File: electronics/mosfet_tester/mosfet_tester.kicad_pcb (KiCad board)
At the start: 2 copper layers, 77 parts, among them J102 CONN_01X06, J103 Screw_Terminal_1x01, J104 Screw_Terminal_1x01, J201 TEST_1P, J202 TEST_1P, J203 TEST_1P, J204 TEST_1P, J205 TEST_1P, J206 TEST_1P, J207 TEST_1P, J301 TEST_1P, J302 TEST_1P, J303 TEST_1P, J304 TEST_1P, J305 TEST_1P, J306 TEST_1P, J307 TEST_1P, J401 TEST_1P, J402 TEST_1P, J403 TEST_1P, J404 TEST_1P, J405 TEST_1P, J406 TEST_1P, J407 TEST_1P, J501 TEST_1P, J502 TEST_1P, J503 TEST_1P, J504 TEST_1P, J505 TEST_1P, J506 TEST_1P, J507 TEST_1P, Q201 Q_NMOS_GSD, Q301 Q_NMOS_GSD, Q401 Q_NMOS_GSD, Q501 Q_NMOS_GSD, U201 LM358, U301 LM358, U401 LM358, U501 LM358

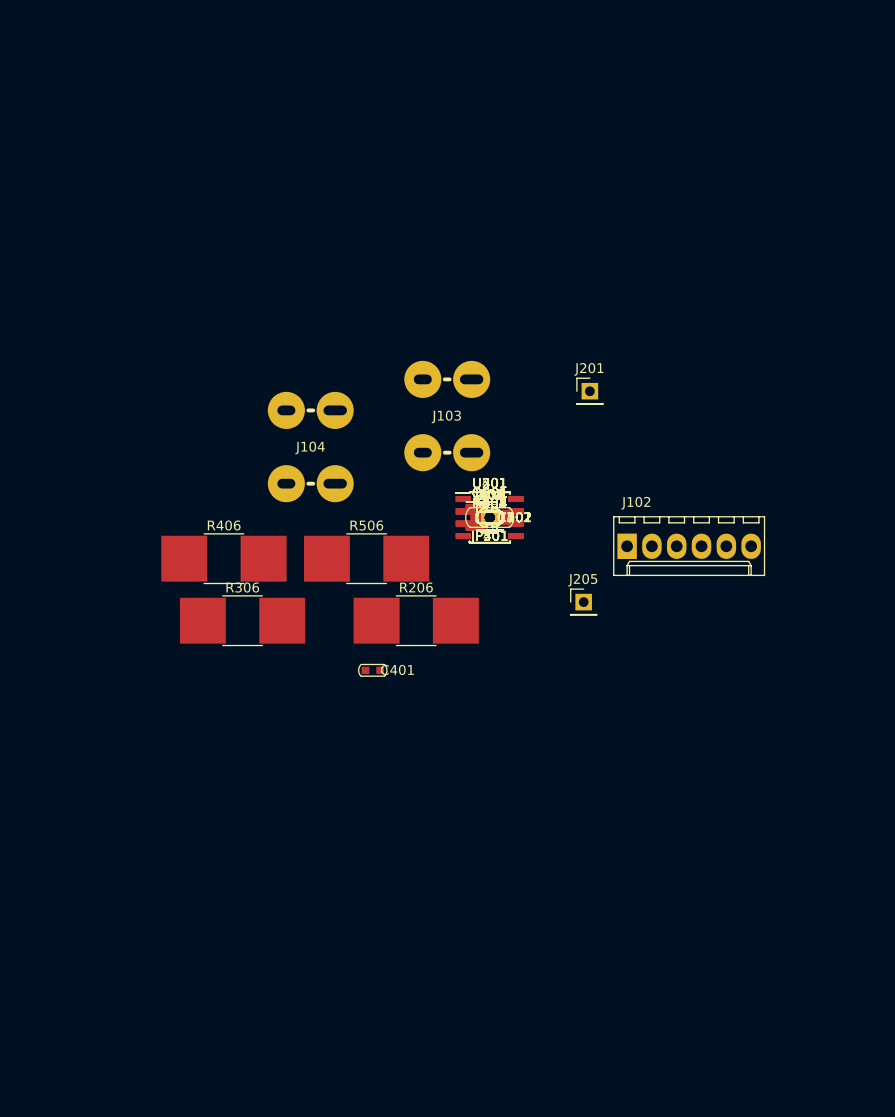
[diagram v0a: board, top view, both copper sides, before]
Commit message: mosfet tester progress
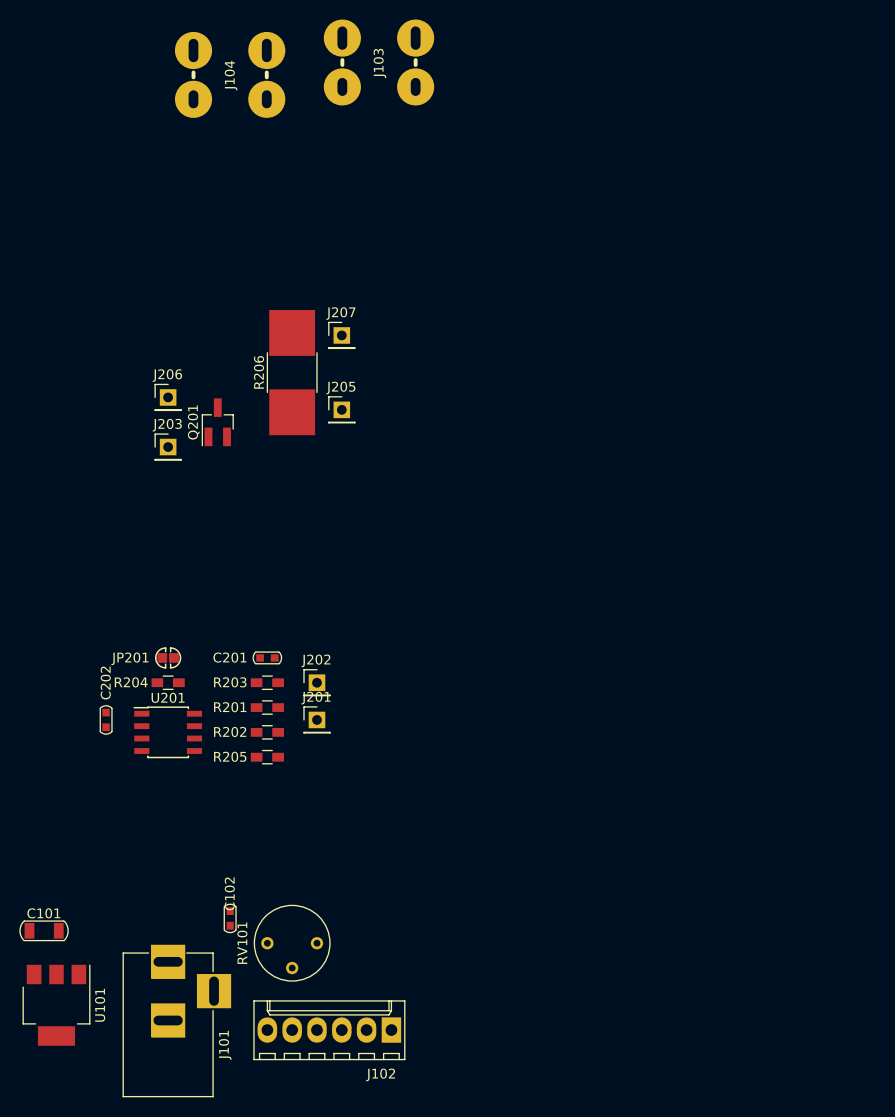
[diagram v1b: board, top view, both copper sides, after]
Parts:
- removed C301, C401, C501: 0.1, Capacitors_SMD_Round:C_0603
- removed C302, C402, C502: C, Capacitors_SMD_Round:C_0603
- removed J204, J301, J302, J303, J304, J305, J306, J307, J401, J402, J403, J404, J405, J406, J407, J501, J502, J503, J504, J505, J506, J507: TEST_1P, Pin_Headers:Pin_Header_Straight_1x01_Pitch2.54mm
- removed JP301, JP401, JP501: Jumper_NC_Small, SolderJumpers:SJ_1_NO
- removed Q301, Q401, Q501: Q_NMOS_GSD, TO_SOT_Packages_SMD:SOT-23_Handsoldering
- removed R301, R401, R501: 100R, Resistors_SMD:R_0603_HandSoldering
- removed R302, R303, R304, R305, R402, R403, R404, R405, R502, R503, R504, R505: R, Resistors_SMD:R_0603_HandSoldering
- removed R306, R406, R506: R, Resistors_SMD:R_2816_HandSoldering
- removed U301, U401, U501: LM358, Housings_SOIC:SOIC-8_3.9x4.9mm_Pitch1.27mm
- added J101: BARREL_JACK, Connectors:BARREL_JACK, F.Cu at (115.6, 150.5)
- added RV101: 10K, Potentiometers:Potentiometer_Trimmer_Bourns_3339P_Horizontal, F.Cu at (130.8, 148.6)
- added U101: LM7805CT, TO_SOT_Packages_SMD:SOT-223-3Lead_TabPin2, F.Cu at (104.1, 154.9)
- C102: value C -> 0.1
- moved C101 62.2 mm to (102.9, 147.3)
- moved J102 55.1 mm to (138.4, 157.5), turned to 180 degrees
- moved C102 48.9 mm to (121.9, 146.1), turned to 90 degrees
- moved C202 44.4 mm to (109.2, 125.7), turned to 270 degrees
- moved J201 43.7 mm to (130.8, 125.7)
- moved U201 39.6 mm to (115.6, 127.0)
- moved J104 39.0 mm to (121.9, 59.7), turned to 90 degrees
- moved R204 37.0 mm to (115.6, 121.9), turned to 180 degrees
- moved J103 36.9 mm to (137.2, 58.4), turned to 90 degrees
- moved JP201 35.9 mm to (115.6, 119.4), turned to 180 degrees
- moved J206 35.2 mm to (115.6, 92.7)
- moved J203 33.7 mm to (115.6, 97.8)
- moved R205 33.5 mm to (125.7, 129.5), turned to 180 degrees
- moved R202 31.7 mm to (125.7, 127.0), turned to 180 degrees
- moved J205 31.6 mm to (133.3, 94.0)
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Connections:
- net /sheet59556740/5V_REF renamed /slice/5V_REF
- C101 pad 1: (no net) -> +5V
- J102 pad 2: /sheet59556740/Vgs -> (no net)
- J102 pad 3: /sheet59556CDB/Vgs -> (no net)
- J102 pad 4: /sheet5955708A/Vgs -> (no net)
- J103 pad 1: /sheet59556740/VIN- -> GND
- J104 pad 1: /sheet59556740/VIN+ -> /slice/VIN+
- J205 pad 1: (no net) -> Net-(J205-Pad1)
- J206 pad 1: (no net) -> /slice/VIN+
- J207 pad 1: (no net) -> GND
- JP201 pad 2: /sheet59556740/VIN- -> GND
- Q201 pad 2: Net-(Q201-Pad2) -> Net-(J205-Pad1)
- Q201 pad 3: /sheet59556740/VIN+ -> /slice/VIN+
- R205 pad 1: Net-(Q201-Pad2) -> Net-(J205-Pad1)
- R206 pad 1: Net-(Q201-Pad2) -> Net-(J205-Pad1)
- R206 pad 2: /sheet59556740/VIN- -> GND

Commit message: Rework entire board, still in progress
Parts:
- removed J206, J207: TEST_1P, Pin_Headers:Pin_Header_Straight_1x01_Pitch2.54mm
- removed JP201: Jumper_NC_Small, SolderJumpers:SJ_1_NO
- added C102: 0.1u, Capacitors_SMD_Round:C_0603, F.Cu at (135.3, 123.2)
- added C301: 0.1, Capacitors_SMD_Round:C_0603, F.Cu at (141.6, 108.0)
- added C302: C, Capacitors_SMD_Round:C_0603, F.Cu at (137.8, 100.3)
- added C401: 0.1, Capacitors_SMD_Round:C_0603, F.Cu at (157.5, 108.0)
- added C402: C, Capacitors_SMD_Round:C_0603, F.Cu at (153.7, 100.3)
- added C501: 0.1, Capacitors_SMD_Round:C_0603, F.Cu at (174.0, 108.0)
- added C502: C, Capacitors_SMD_Round:C_0603, F.Cu at (170.2, 100.3)
- added J301: TEST_1P, Pin_Headers:Pin_Header_Straight_1x01_Pitch2.54mm, F.Cu at (142.2, 113.0)
- added J302: TEST_1P, Pin_Headers:Pin_Header_Straight_1x01_Pitch2.54mm, F.Cu at (147.3, 113.0)
- added J303: TEST_1P, Pin_Headers:Pin_Header_Straight_1x01_Pitch2.54mm, F.Cu at (142.2, 118.7)
- added J304: TEST_1P, Pin_Headers:Pin_Header_Straight_1x01_Pitch2.54mm, F.Cu at (147.3, 118.7)
- added J401: TEST_1P, Pin_Headers:Pin_Header_Straight_1x01_Pitch2.54mm, F.Cu at (158.1, 113.0)
- added J402: TEST_1P, Pin_Headers:Pin_Header_Straight_1x01_Pitch2.54mm, F.Cu at (163.2, 113.0)
- added J403: TEST_1P, Pin_Headers:Pin_Header_Straight_1x01_Pitch2.54mm, F.Cu at (158.1, 118.7)
- added J404: TEST_1P, Pin_Headers:Pin_Header_Straight_1x01_Pitch2.54mm, F.Cu at (163.2, 118.7)
- added J501: TEST_1P, Pin_Headers:Pin_Header_Straight_1x01_Pitch2.54mm, F.Cu at (174.6, 113.0)
- added J502: TEST_1P, Pin_Headers:Pin_Header_Straight_1x01_Pitch2.54mm, F.Cu at (179.7, 113.0)
- added J503: TEST_1P, Pin_Headers:Pin_Header_Straight_1x01_Pitch2.54mm, F.Cu at (174.6, 118.7)
- added J504: TEST_1P, Pin_Headers:Pin_Header_Straight_1x01_Pitch2.54mm, F.Cu at (179.7, 118.7)
- added P101: OSHW, Symbols:OSHW-Logo_7.5x8mm_SilkScreen, F.Cu at (137.2, 93.3)
- added Q301: Q_NMOS_GSD, TO_Combo_Packages:TO_220_247, F.Cu at (141.6, 79.4)
- added Q401: Q_NMOS_GSD, TO_Combo_Packages:TO_220_247, B.Cu at (157.5, 79.4)
- added Q501: Q_NMOS_GSD, TO_Combo_Packages:TO_220_247, F.Cu at (174.0, 79.4)
- added R101: 0R, Resistors_SMD:R_0805_HandSoldering, F.Cu at (186.1, 97.8)
- added R301: 100R, Resistors_SMD:R_0603_HandSoldering, F.Cu at (148.0, 101.6)
- added R302: R, Resistors_SMD:R_0603_HandSoldering, F.Cu at (148.0, 103.5)
- added R303: R, Resistors_SMD:R_0603_HandSoldering, F.Cu at (148.0, 105.4)
- added R304: R, Resistors_THT:R_Axial_DIN0207_L6.3mm_D2.5mm_P10.16mm_Horizontal, F.Cu at (144.8, 89.5)
- added R305: R, Resistors_THT:R_Axial_DIN0207_L6.3mm_D2.5mm_P10.16mm_Horizontal, F.Cu at (148.0, 89.5)
- added R306: R, Resistors_SMD:R_2816_HandSoldering, F.Cu at (146.1, 85.7)
- added R401: 100R, Resistors_SMD:R_0603_HandSoldering, F.Cu at (163.8, 101.6)
- added R402: R, Resistors_SMD:R_0603_HandSoldering, F.Cu at (163.8, 103.5)
- added R403: R, Resistors_SMD:R_0603_HandSoldering, F.Cu at (163.8, 105.4)
- added R404: R, Resistors_THT:R_Axial_DIN0207_L6.3mm_D2.5mm_P10.16mm_Horizontal, F.Cu at (160.7, 89.5)
- added R405: R, Resistors_THT:R_Axial_DIN0207_L6.3mm_D2.5mm_P10.16mm_Horizontal, F.Cu at (163.8, 89.5)
- added R406: R, Resistors_SMD:R_2816_HandSoldering, F.Cu at (161.9, 85.7)
- added R501: 100R, Resistors_SMD:R_0603_HandSoldering, F.Cu at (181.0, 101.6)
- added R502: R, Resistors_SMD:R_0603_HandSoldering, F.Cu at (181.0, 103.5)
- added R503: R, Resistors_SMD:R_0603_HandSoldering, F.Cu at (181.0, 105.4)
- added R504: R, Resistors_THT:R_Axial_DIN0207_L6.3mm_D2.5mm_P10.16mm_Horizontal, F.Cu at (177.2, 89.5)
- added R505: R, Resistors_THT:R_Axial_DIN0207_L6.3mm_D2.5mm_P10.16mm_Horizontal, F.Cu at (180.3, 89.5)
- added R506: R, Resistors_SMD:R_2816_HandSoldering, F.Cu at (178.4, 85.7)
- added U301: LM358, Housings_SOIC:SOIC-8_3.9x4.9mm_Pitch1.27mm, F.Cu at (141.6, 104.1)
- added U401: LM358, Housings_SOIC:SOIC-8_3.9x4.9mm_Pitch1.27mm, F.Cu at (157.5, 104.1)
- added U501: LM358, Housings_SOIC:SOIC-8_3.9x4.9mm_Pitch1.27mm, F.Cu at (174.0, 104.1)
- C101: value C -> 22u
- J102: value CONN_01X06 -> CONN_01X03; footprint Connectors_Molex:Molex_KK-6410-06_06x2.54mm_Straight -> Connectors_Molex:Molex_KK-6410-03_03x2.54mm_Straight
- J103, J104: footprint Screw_Connectors:4_Pin_Screw_Connector -> Screw_Connectors:2_Pin_Quick_Fit
- Q201: footprint TO_SOT_Packages_SMD:SOT-23_Handsoldering -> TO_Combo_Packages:TO_220_247; moved to B.Cu
- R204, R205: footprint Resistors_SMD:R_0603_HandSoldering -> Resistors_THT:R_Axial_DIN0207_L6.3mm_D2.5mm_P10.16mm_Horizontal
- RV101: footprint Potentiometers:Potentiometer_Trimmer_Bourns_3339P_Horizontal -> Potentiometers:Potentiometer_Alps_RK163_Double_Vertical
- U101: value LM7805CT -> MCP1703A-3302/MB; footprint TO_SOT_Packages_SMD:SOT-223-3Lead_TabPin2 -> TO_SOT_Packages_SMD:SOT89-3_Housing
- moved J102 43.5 mm to (120.0, 118.1), turned to 90 degrees
- moved U101 40.6 mm to (135.3, 128.9), turned to 180 degrees
- moved R205 40.5 mm to (132.1, 89.5), turned to 270 degrees
- moved C101 39.3 mm to (135.3, 125.1), turned to 180 degrees
- moved J104 36.2 mm to (122.6, 95.9), turned to 0 degrees
- moved R204 35.0 mm to (128.9, 89.5), turned to 270 degrees
- moved J103 33.9 mm to (120.0, 87.6), turned to 270 degrees
- moved C202 28.4 mm to (121.9, 100.3), turned to 180 degrees
- moved C103 25.5 mm to (142.9, 131.4)
- moved U201 25.0 mm to (125.7, 104.1)
- moved J204 24.8 mm to (131.4, 118.7)
- moved J101 24.7 mm to (126.4, 128.3), turned to 0 degrees
- moved R202 24.3 mm to (132.1, 103.5)
- moved R201 23.7 mm to (132.1, 101.6)
- moved J203 23.6 mm to (126.4, 118.7)
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- renumbered C102 to C103, J205 to J204
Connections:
- C103 pad 1: /slice/5V_REF -> /slice1/5V_REF
- C202 pad 1: Net-(C202-Pad1) -> /slice1/Vgs
- J102 pad 1: /slice/Vgs -> +12V
- J102 pad 2: (no net) -> /slice1/5V_REF
- J102 pad 3: (no net) -> GND
- J103 pad 1: GND -> /slice1/VIN+
- J104 pad 1: /slice/VIN+ -> /slice1/VIN-
- J203 pad 1: /slice/Vgs -> /slice1/Vgs
- J204 pad 1: Net-(J205-Pad1) -> Net-(J204-Pad1)
- Q201 pad 1: /slice/Vgs -> Net-(Q201-Pad1)
- Q201 pad 2: Net-(J205-Pad1) -> Net-(Q201-Pad2)
- Q201 pad 3: /slice/VIN+ -> /slice1/VIN+
- R203 pad 1: Net-(JP201-Pad1) -> /slice1/VIN-
- R204 pad 1: /slice/Vgs -> Net-(Q201-Pad2)
- R204 pad 2: Net-(C202-Pad1) -> Net-(J204-Pad1)
- R205 pad 1: Net-(J205-Pad1) -> Net-(Q201-Pad1)
- R205 pad 2: Net-(R205-Pad2) -> /slice1/Vgs
- R206 pad 1: Net-(J205-Pad1) -> Net-(Q201-Pad2)
- R206 pad 2: GND -> /slice1/VIN-
- RV101 pad 2: /slice/5V_REF -> /slice1/5V_REF
- U101 pad 1: +12V -> GND
- U101 pad 2: GND -> +12V
- U201 pad 1: Net-(C202-Pad1) -> /slice1/Vgs
- U201 pad 3: /slice/5V_REF -> /slice1/5V_REF
- U201 pad 5: Net-(R205-Pad2) -> Net-(J204-Pad1)
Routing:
- net +12V: track 0.00 -> 111.5 mm, vias 0 -> 4
- net /slice1/5V_REF: track 0.00 -> 106.8 mm, vias 0 -> 2
- net /slice1/VIN+: track 0.00 -> 96.7 mm
- net GND: track 0.00 -> 69.2 mm
- net /slice1/VIN-: track 0.00 -> 34.1 mm
- net /slice1/Vgs: track 0.00 -> 30.0 mm, vias 0 -> 1
- net /slice2/Vgs: track 0.00 -> 29.5 mm, vias 0 -> 1
- net /slice3/Vgs: track 0.00 -> 29.5 mm, vias 0 -> 1
- net /slice4/Vgs: track 0.00 -> 29.5 mm, vias 0 -> 1
- net Net-(C502-Pad2): track 0.00 -> 23.0 mm, vias 0 -> 1
- net Net-(J404-Pad1): track 0.00 -> 22.9 mm, vias 0 -> 1
- net Net-(J204-Pad1): track 0.00 -> 22.9 mm, vias 0 -> 1
- net Net-(C202-Pad2): track 0.00 -> 22.6 mm, vias 0 -> 1
- net Net-(C402-Pad2): track 0.00 -> 22.3 mm, vias 0 -> 1
- net Net-(C302-Pad2): track 0.00 -> 22.3 mm, vias 0 -> 1
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- added copper zone on B.Cu, net /slice1/VIN+
- added copper zone on F.Cu, net /slice1/VIN-
- added copper zone on F.Cu, net GND
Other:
- board outline added: 71.8 x 60.3 mm

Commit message: Checkpoint mosfet tester
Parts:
- removed J102: CONN_01X03, Connectors_Molex:Molex_KK-6410-03_03x2.54mm_Straight
- removed U101: MCP1703A-3302/MB, TO_SOT_Packages_SMD:SOT89-3_Housing
- added J1: CONN_01X03, Connectors_Molex:Molex_KK-6410-03_03x2.54mm_Straight, F.Cu at (120.0, 116.2)
- added M1: BuckModule, Buck_Modules:Buck_Module_7805_Replacement_Universal, F.Cu at (167.0, 123.2)
- moved C101 34.7 mm to (168.9, 116.8)
- moved P101 31.1 mm to (136.5, 124.5)
- moved C102 19.3 mm to (153.7, 117.5)
- moved C103 19.2 mm to (153.7, 115.6), turned to 0 degrees
- moved RV101 5.71 mm to (148.0, 127.6)
- moved J101 4.45 mm to (126.4, 123.8)
- moved J203 1.91 mm to (126.4, 116.8)
- moved J204 1.91 mm to (131.4, 116.8)
- moved J303 1.91 mm to (142.2, 116.8)
- moved J304 1.91 mm to (147.3, 116.8)
- moved J403 1.91 mm to (158.1, 116.8)
- moved J404 1.91 mm to (163.2, 116.8)
- moved J503 1.91 mm to (174.6, 116.8)
- moved J504 1.91 mm to (179.7, 116.8)
- moved J201 1.27 mm to (126.4, 111.8)
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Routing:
- net GND: track 69.2 -> 13.1 mm
- net +12V: track 111.5 -> 143.4 mm
- net /slice1/5V_REF: track 106.8 -> 90.8 mm, vias 2 -> 3
- net +5V: track 18.2 -> 33.0 mm, vias 0 -> 1
- net /slice1/VIN+: track 96.7 -> 103.6 mm
- net Net-(J504-Pad1): track 21.6 -> 19.7 mm
- net Net-(J404-Pad1): track 22.9 -> 21.0 mm
- net Net-(J304-Pad1): track 22.0 -> 20.1 mm
- net Net-(J204-Pad1): track 22.9 -> 21.0 mm
- net /slice4/Vgs: track 29.5 -> 27.6 mm
- net /slice3/Vgs: track 29.5 -> 27.6 mm
- net /slice1/Vgs: track 30.0 -> 28.1 mm
- net /slice2/Vgs: track 29.5 -> 27.6 mm
- net Net-(C402-Pad2): track 22.3 -> 21.1 mm
- net Net-(C202-Pad2): track 22.6 -> 21.3 mm
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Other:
- board size 71.8 x 60.3 mm -> 71.8 x 54.6 mm
- board text added: "CC-BY"
- board text added: "github.com/google/ makerspace-partsbin electronics/mosfet_tester"
- board text added: "mosfet tester v1"
